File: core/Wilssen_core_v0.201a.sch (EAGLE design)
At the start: 28 parts, among them Q1 8Mhz, U1 MAX1555, U2 3.3V, U3 ATMEGA168/ATMEGA328, X1 USBSMD

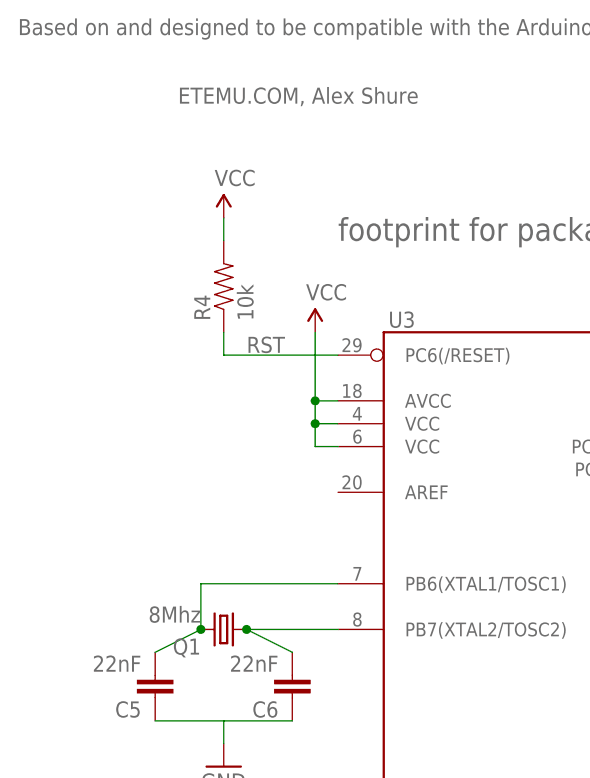
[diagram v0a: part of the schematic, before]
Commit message: added external voltage reference
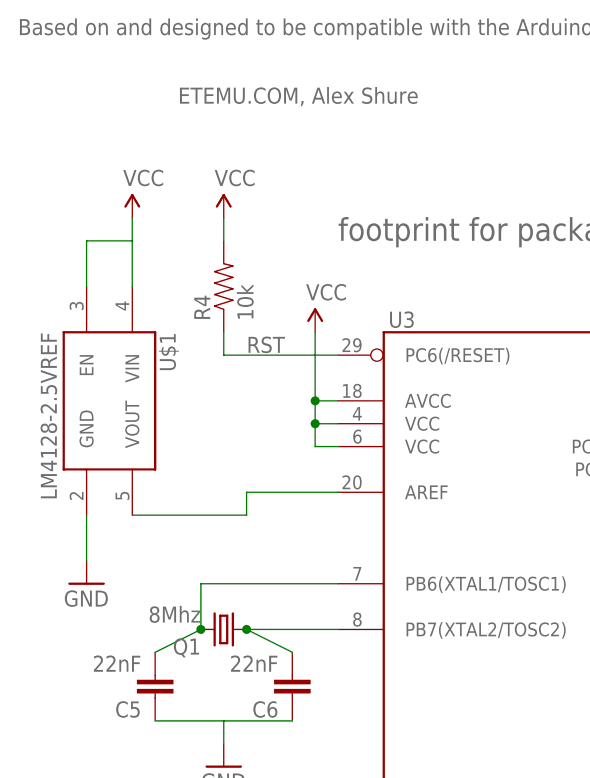
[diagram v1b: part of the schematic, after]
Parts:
- added U$1: LM4128-2.5VREF, SparkFun-PowerIC:LM4128-2.5VREF
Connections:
- new net N$3: U$1.VOUT, U3.AREF
- net GND: now also U$1.GND
- net VCC: now also U$1.EN, U$1.VIN
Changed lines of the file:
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@@
 <grid distance="0.1" unitdist="inch" unit="inch" style="lines" multiple="1" display="no" altdistance="0.01" altunitdist="inch" altunit="inch"/>
 <layers>
-<layer number="1" name="Top" color="4" fill="1" visible="no" active="no"/>
-<layer number="2" name="Route2" color="1" fill="3" visible="no" active="no"/>
-<layer number="3" name="Route3" color="4" fill="3" visible="no" active="no"/>
-<layer number="4" name="Route4" color="1" fill="4" visible="no" active="no"/>
-<layer number="5" name="Route5" color="4" fill="4" visible="no" active="no"/>
-<layer number="6" name="Route6" color="1" fill="8" visible="no" active="no"/>
-<layer number="7" name="Route7" color="4" fill="8" visible="no" active="no"/>
-<layer number="8" name="Route8" color="1" fill="2" visible="no" active="no"/>
-<layer number="9" name="Route9" color="4" fill="2" visible="no" active="no"/>
-<layer number="10" name="Route10" color="1" fill="7" visible="no" active="no"/>
-<layer number="11" name="Route11" color="4" fill="7" visible="no" active="no"/>
-<layer number="12" name="Route12" color="1" fill="5" visible="no" active="no"/>
-<layer number="13" name="Route13" color="4" fill="5" visible="no" active="no"/>
-<layer number="14" name="Route14" color="1" fill="6" visible="no" active="no"/>
-<layer number="15" name="Route15" color="4" fill="6" visible="no" active="no"/>
-<layer number="16" name="Bottom" color="1" fill="1" visible="no" active="no"/>
-<layer number="17" name="Pads" color="2" fill="1" visible="no" active="no"/>
-<layer number="18" name="Vias" color="2" fill="1" visible="no" active="no"/>
-<layer number="19" name="Unrouted" color="6" fill="1" visible="no" active="no"/>
-<layer number="20" name="Dimension" color="6" fill="1" visible="no" active="no"/>
-<layer number="21" name="tPlace" color="16" fill="1" visible="no" active="no"/>
-<layer number="22" name="bPlace" color="14" fill="1" visible="no" active="no"/>
-<layer number="23" name="tOrigins" color="15" fill="1" visible="no" active="no"/>
-<layer number="24" name="bOrigins" color="15" fill="1" visible="no" active="no"/>
-<layer number="25" name="tNames" color="7" fill="1" visible="no" active="no"/>
-<layer number="26" name="bNames" color="7" fill="1" visible="no" active="no"/>
-<layer number="27" name="tValues" color="7" fill="1" visible="no" active="no"/>
-<layer number="28" name="bValues" color="7" fill="1" visible="no" active="no"/>
+<layer number="1" name="Top" color="4" fill="1" visible="yes" active="no"/>
+<layer number="2" name="Route2" color="1" fill="3" visible="yes" active="no"/>
+<layer number="3" name="Route3" color="4" fill="3" visible="yes" active="no"/>
+<layer number="4" name="Route4" color="1" fill="4" visible="yes" active="no"/>
+<layer number="5" name="Route5" color="4" fill="4" visible="yes" active="no"/>
+<layer number="6" name="Route6" color="1" fill="8" visible="yes" active="no"/>
+<layer number="7" name="Route7" color="4" fill="8" visible="yes" active="no"/>
+<layer number="8" name="Route8" color="1" fill="2" visible="yes" active="no"/>
+<layer number="9" name="Route9" color="4" fill="2" visible="yes" active="no"/>
+<layer number="10" name="Route10" color="1" fill="7" visible="yes" active="no"/>
+<layer number="11" name="Route11" color="4" fill="7" visible="yes" active="no"/>
+<layer number="12" name="Route12" color="1" fill="5" visible="yes" active="no"/>
+<layer number="13" name="Route13" color="4" fill="5" visible="yes" active="no"/>
+<layer number="14" name="Route14" color="1" fill="6" visible="yes" active="no"/>
+<layer number="15" name="Route15" color="4" fill="6" visible="yes" active="no"/>
+<layer number="16" name="Bottom" color="1" fill="1" visible="yes" active="no"/>
+<layer number="17" name="Pads" color="2" fill="1" visible="yes" active="no"/>
+<layer number="18" name="Vias" color="2" fill="1" visible="yes" active="no"/>
+<layer number="19" name="Unrouted" color="6" fill="1" visible="yes" active="no"/>
+<layer number="20" name="Dimension" color="6" fill="1" visible="yes" active="no"/>
+<layer number="21" name="tPlace" color="16" fill="1" visible="yes" active="no"/>
+<layer number="22" name="bPlace" color="14" fill="1" visible="yes" active="no"/>
+<layer number="23" name="tOrigins" color="15" fill="1" visible="yes" active="no"/>
+<layer number="24" name="bOrigins" color="15" fill="1" visible="yes" active="no"/>
+<layer number="25" name="tNames" color="7" fill="1" visible="yes" active="no"/>
+<layer number="26" name="bNames" color="7" fill="1" visible="yes" active="no"/>
+<layer number="27" name="tValues" color="7" fill="1" visible="yes" active="no"/>
+<layer number="28" name="bValues" color="7" fill="1" visible="yes" active="no"/>
 <layer number="29" name="tStop" color="5" fill="1" visible="no" active="no"/>
 <layer number="30" name="bStop" color="7" fill="6" visible="no" active="no"/>
@@
 <layer number="35" name="tGlue" color="7" fill="4" visible="no" active="no"/>
 <layer number="36" name="bGlue" color="7" fill="5" visible="no" active="no"/>
-<layer number="37" name="tTest" color="7" fill="1" visible="no" active="no"/>
-<layer number="38" name="bTest" color="7" fill="1" visible="no" active="no"/>
+<layer number="37" name="tTest" color="7" fill="1" visible="yes" active="no"/>
+<layer number="38" name="bTest" color="7" fill="1" visible="yes" active="no"/>
 <layer number="39" name="tKeepout" color="4" fill="11" visible="no" active="no"/>
 <layer number="40" name="bKeepout" color="1" fill="11" visible="no" active="no"/>
@@
 <layer number="44" name="Drills" color="7" fill="1" visible="no" active="no"/>
 <layer number="45" name="Holes" color="7" fill="1" visible="no" active="no"/>
-<layer number="46" name="Milling" color="3" fill="1" visible="no" active="no"/>
-<layer number="47" name="Measures" color="7" fill="1" visible="no" active="no"/>
-<layer number="48" name="Document" color="7" fill="1" visible="no" active="no"/>
-<layer number="49" name="Reference" color="7" fill="1" visible="no" active="no"/>
-<layer number="50" name="dxf" color="7" fill="1" visible="no" active="no"/>
-<layer number="51" name="tDocu" color="6" fill="1" visible="no" active="no"/>
-<layer number="52" name="bDocu" color="7" fill="1" visible="no" active="no"/>
-<layer number="53" name="tGND_GNDA" color="7" fill="9" visible="no" active="no"/>
-<layer number="54" name="bGND_GNDA" color="1" fill="9" visible="no" active="no"/>
-<layer number="56" name="wert" color="7" fill="1" visible="no" active="no"/>
+<layer number="46" name="Milling" color="3" fill="1" visible="yes" active="no"/>
+<layer number="47" name="Measures" color="7" fill="1" visible="yes" active="no"/>
+<layer number="48" name="Document" color="7" fill="1" visible="yes" active="no"/>
+<layer number="49" name="Reference" color="7" fill="1" visible="yes" active="no"/>
+<layer number="50" name="dxf" color="7" fill="1" visible="yes" active="no"/>
+<layer number="51" name="tDocu" color="6" fill="1" visible="yes" active="no"/>
+<layer number="52" name="bDocu" color="7" fill="1" visible="yes" active="no"/>
+<layer number="53" name="tGND_GNDA" color="7" fill="9" visible="yes" active="no"/>
+<layer number="54" name="bGND_GNDA" color="1" fill="9" visible="yes" active="no"/>
+<layer number="56" name="wert" color="7" fill="1" visible="yes" active="no"/>
 <layer number="91" name="Nets" color="2" fill="1" visible="yes" active="yes"/>
 <layer number="92" name="Busses" color="1" fill="1" visible="yes" active="yes"/>
@@
 <part name="JP9" library="SparkFun-Connectors" deviceset="M06" device="SIP"/>
 <part name="R5" library="rcl" deviceset="R-EU_" device="R1206" value="3R3"/>
+<part name="U$1" library="SparkFun-PowerIC" deviceset="LM4128-2.5VREF" device=""/>
+<part name="GND6" library="SparkFun" deviceset="GND" device=""/>
+<part name="P+6" library="SparkFun" deviceset="VCC" device=""/>
 </parts>
 <sheets>
@@
 <instance part="JP9" gate="G$1" x="139.7" y="162.56" rot="R180"/>
 <instance part="R5" gate="G$1" x="129.54" y="17.78"/>
+<instance part="U$1" gate="G$1" x="12.7" y="139.7" rot="R270"/>
+<instance part="GND6" gate="1" x="10.16" y="119.38"/>
+<instance part="P+6" gate="1" x="15.24" y="160.02" smashed="yes">
+<attribute name="VALUE" x="14.224" y="163.576" size="1.778" layer="96"/>
+</instance>
 </instances>
 <busses>
@@
 <pinref part="GND14" gate="1" pin="GND"/>
 <wire x1="165.1" y1="139.7" x2="165.1" y2="132.08" width="0.1524" layer="91"/>
+</segment>
+<segment>
+<pinref part="U$1" gate="G$1" pin="GND"/>
+<pinref part="GND6" gate="1" pin="GND"/>
+<wire x1="10.16" y1="121.92" x2="10.16" y2="127" width="0.1524" layer="91"/>
 </segment>
 </net>
@@
 <wire x1="175.26" y1="134.62" x2="172.72" y2="134.62" width="0.1524" layer="91"/>
 <pinref part="ATMEGA168/ATMEGA328" gate="G$1" pin="AREF"/>
+</segment>
+<segment>
+<pinref part="U$1" gate="G$1" pin="VIN"/>
+<pinref part="P+6" gate="1" pin="VCC"/>
+<wire x1="15.24" y1="160.02" x2="15.24" y2="157.48" width="0.1524" layer="91"/>
+<pinref part="U$1" gate="G$1" pin="EN"/>
+<wire x1="15.24" y1="157.48" x2="15.24" y2="152.4" width="0.1524" layer="91"/>
+<wire x1="10.16" y1="152.4" x2="10.16" y2="157.48" width="0.1524" layer="91"/>
+<wire x1="10.16" y1="157.48" x2="15.24" y2="157.48" width="0.1524" layer="91"/>
 </segment>
 </net>
@@
 </segment>
 </net>
+<net name="N$3" class="0">
+<segment>
+<pinref part="U$1" gate="G$1" pin="VOUT"/>
+<wire x1="15.24" y1="127" x2="27.94" y2="127" width="0.1524" layer="91"/>
+<wire x1="27.94" y1="127" x2="27.94" y2="129.54" width="0.1524" layer="91"/>
+<pinref part="U3" gate="G$1" pin="AREF"/>
+<wire x1="27.94" y1="129.54" x2="38.1" y2="129.54" width="0.1524" layer="91"/>
+</segment>
+</net>
